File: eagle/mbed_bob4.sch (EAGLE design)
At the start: 15 parts, among them IC1 MBED-SOCKET, K1 651005136521, K2 691210910006, K3 691210910006, T1 2N7002E

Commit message: First working version. To be cleaned up and checked before sending out for production.
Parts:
- added IC2: MAX9934, ic:MAX9934
- added K4: 691210910006, Wuerth_Elektronik_eiCan_14_Terminal_Blocks_WR-TBL_2_0:691210910006
- added R8: R_KELVIN, passives:R_KELVIN
- added X1: SDCARDSHORT, connectors:SDCARDSHORT
- ETH1: value CON-RJ45-F -> CON-RJ45-F_WE100; device dp_devices:CON-RJ45-F -> connectors:CON-RJ45-F_WE100
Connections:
- new net CAN_RX: IC1.30, K4.1
- new net CAN_TX: IC1.29, K4.2
- new net MAX_CS: IC1.22, IC2.CS
- new net N$14: IC1.7, X1.SCK
- new net N$15: IC1.8, X1.CS
- new net N$16: IC1.5, X1.DI
- new net N$17: IC1.6, X1.DO
- new net N$18: IC1.VB
- new net N$19: IC1.NR
- new net N$20: IC1.11
- new net N$21: IC1.12
- new net N$22: IC1.13
- new net N$23: IC1.15
- new net N$24: IC1.16, IC2.OUT
- new net N$25: K3.3, R8.I1
- new net N$26: IC1.23
- new net N$27: IC1.24
- new net N$28: IC1.IF+
- new net N$29: IC1.IF-
- new net N$30: IC1.VU
- new net N$31: IC2.RS-, R8.V2
- new net N$32: IC2.RS+, R8.V1
- new net N$33: K3.4, R8.I2
- new net PWM25: IC1.25, K4.6
- new net PWM26: IC1.26, K4.5
- new net SCL: IC1.27, K4.4
- new net SDA: IC1.28, K4.3
- net +3V3: now also ETH1.CRD, ETH1.CTD, IC2.VCC, X1.VCC; no longer ETH1.4, ETH1.5
- net GND: now also ETH1.GREEN_CATHODE, ETH1.SHIELD, ETH1.YELLOW_CATHODE, IC2.GND, RN2A.1, RN2B.1, RN2C.1, RN2D.1, X1.GND; no longer ETH1.10, ETH1.11
- net LED1: now also IC1.9
- net LED2: now also IC1.10
- net N$1: now also RN2D.2; no longer RN2A.2
- net N$11: now also ETH1.GREEN_ANODE; no longer ETH1.12
- net N$12: now also ETH1.YELLOW_ANODE; no longer ETH1.9
- net N$3: now also IC1.14, X1.CD; no longer RN2A.1, RN2B.1, RN2C.1, RN2D.1
- net N$5: now also RN2A.2; no longer RN2D.2
- net N$6: now also RN2B.2; no longer RN2C.2
- net N$7: now also RN2C.2; no longer RN2B.2
- net RX_N: now also ETH1.RD-; no longer ETH1.6
- net RX_P: now also ETH1.RD+; no longer ETH1.3
- net TX_N: now also ETH1.TD-; no longer ETH1.2
- net TX_P: now also ETH1.TD+; no longer ETH1.1
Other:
- moved on the sheet: ETH1, K1, K2, R1, RN2A, RN2B, RN2C, RN2D, T1

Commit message: Further cleanup
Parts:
- renumbered K1 to USB
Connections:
- removed net N$2: USB.GND
- net +3V3: now also K3.1
- net GND: now also USB.GND
- net N$13: now also K3.4
- net N$25: now also K3.2; no longer K3.3
- net N$33: now also K3.3; no longer K3.4
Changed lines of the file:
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@@
 <parts>
 <part name="FRAME1" library="frames" deviceset="A4L-LOC" device=""/>
-<part name="K1" library="Wuerth_Elektronik_eiCan_11_Communication_Connectors_2_4" deviceset="651005136521" device=""/>
+<part name="USB" library="Wuerth_Elektronik_eiCan_11_Communication_Connectors_2_4" deviceset="651005136521" device=""/>
 <part name="ETH1" library="connectors" deviceset="CON-RJ45-F" device="_WE100"/>
 <part name="GND11" library="mbed-power" deviceset="GND" device=""/>
@@
 <instances>
 <instance part="FRAME1" gate="G$1" x="0" y="0"/>
-<instance part="K1" gate="G$1" x="218.44" y="60.96" rot="MR0"/>
+<instance part="USB" gate="G$1" x="218.44" y="60.96" rot="MR0"/>
 <instance part="ETH1" gate="ETH" x="48.26" y="134.62" rot="MR0"/>
 <instance part="GND11" gate="1" x="228.6" y="48.26" rot="MR0"/>
@@
 <net name="USB_D_N" class="0">
 <segment>
-<pinref part="K1" gate="G$1" pin="D-"/>
+<pinref part="USB" gate="G$1" pin="D-"/>
 <wire x1="226.06" y1="63.5" x2="238.76" y2="63.5" width="0.1524" layer="91"/>
 <label x="231.14" y="63.5" size="1.778" layer="95"/>
@@
 </segment>
 </net>
-<net name="N$2" class="0">
-<segment>
-<pinref part="K1" gate="G$1" pin="GND"/>
-<wire x1="226.06" y1="55.88" x2="228.6" y2="55.88" width="0.1524" layer="91"/>
-</segment>
-</net>
 <net name="USB_D_P" class="0">
 <segment>
-<pinref part="K1" gate="G$1" pin="D+"/>
+<pinref part="USB" gate="G$1" pin="D+"/>
 <wire x1="226.06" y1="60.96" x2="238.76" y2="60.96" width="0.1524" layer="91"/>
 <label x="231.14" y="60.96" size="1.778" layer="95"/>
@@
 <net name="VBUS" class="0">
 <segment>
-<pinref part="K1" gate="G$1" pin="VCC"/>
+<pinref part="USB" gate="G$1" pin="VCC"/>
 <wire x1="226.06" y1="66.04" x2="238.76" y2="66.04" width="0.1524" layer="91"/>
 <label x="231.14" y="66.04" size="1.778" layer="95"/>
@@
 </net>
 <net name="GND" class="0">
-<segment>
-<wire x1="228.6" y1="48.26" x2="228.6" y2="55.88" width="0.1524" layer="91"/>
-<pinref part="GND11" gate="1" pin="GND"/>
-</segment>
 <segment>
 <wire x1="195.58" y1="152.4" x2="190.5" y2="152.4" width="0.1524" layer="91"/>
@@
 <wire x1="114.3" y1="48.26" x2="114.3" y2="50.8" width="0.1524" layer="91"/>
 </segment>
+<segment>
+<pinref part="GND11" gate="1" pin="GND"/>
+<wire x1="228.6" y1="48.26" x2="228.6" y2="55.88" width="0.1524" layer="91"/>
+<pinref part="USB" gate="G$1" pin="GND"/>
+<wire x1="228.6" y1="55.88" x2="226.06" y2="55.88" width="0.1524" layer="91"/>
+</segment>
 </net>
 <net name="+3V3" class="0">
@@
 <wire x1="114.3" y1="73.66" x2="114.3" y2="76.2" width="0.1524" layer="91"/>
 </segment>
+<segment>
+<pinref part="K3" gate="G$1" pin="1"/>
+<pinref part="V3" gate="+3V3" pin="+3V3"/>
+<wire x1="15.24" y1="71.12" x2="17.78" y2="71.12" width="0.1524" layer="91"/>
+<wire x1="17.78" y1="71.12" x2="17.78" y2="76.2" width="0.1524" layer="91"/>
+</segment>
 </net>
 <net name="LGC_IN_LV" class="0">
@@
 <pinref part="T1" gate="A" pin="G"/>
 <pinref part="K3" gate="G$1" pin="5"/>
-<wire x1="15.24" y1="60.96" x2="22.86" y2="60.96" width="0.1524" layer="91"/>
+<wire x1="15.24" y1="60.96" x2="17.78" y2="60.96" width="0.1524" layer="91"/>
+<wire x1="17.78" y1="60.96" x2="22.86" y2="60.96" width="0.1524" layer="91"/>
 <wire x1="22.86" y1="60.96" x2="22.86" y2="22.86" width="0.1524" layer="91"/>
 <wire x1="22.86" y1="22.86" x2="25.4" y2="22.86" width="0.1524" layer="91"/>
+<pinref part="K3" gate="G$1" pin="4"/>
+<wire x1="15.24" y1="63.5" x2="17.78" y2="63.5" width="0.1524" layer="91"/>
+<wire x1="17.78" y1="63.5" x2="17.78" y2="60.96" width="0.1524" layer="91"/>
+<junction x="17.78" y="60.96"/>
 </segment>
 </net>
@@
 <net name="N$25" class="0">
 <segment>
-<pinref part="K3" gate="G$1" pin="3"/>
-<wire x1="15.24" y1="66.04" x2="40.64" y2="66.04" width="0.1524" layer="91"/>
-<wire x1="40.64" y1="66.04" x2="40.64" y2="73.66" width="0.1524" layer="91"/>
 <pinref part="R8" gate="G$1" pin="I1"/>
+<wire x1="40.64" y1="68.58" x2="40.64" y2="73.66" width="0.1524" layer="91"/>
 <wire x1="40.64" y1="73.66" x2="48.26" y2="73.66" width="0.1524" layer="91"/>
+<pinref part="K3" gate="G$1" pin="2"/>
+<wire x1="15.24" y1="68.58" x2="40.64" y2="68.58" width="0.1524" layer="91"/>
 </segment>
 </net>
@@
 <wire x1="73.66" y1="73.66" x2="73.66" y2="60.96" width="0.1524" layer="91"/>
 <wire x1="73.66" y1="60.96" x2="27.94" y2="60.96" width="0.1524" layer="91"/>
-<wire x1="27.94" y1="60.96" x2="27.94" y2="63.5" width="0.1524" layer="91"/>
-<pinref part="K3" gate="G$1" pin="4"/>
-<wire x1="27.94" y1="63.5" x2="15.24" y2="63.5" width="0.1524" layer="91"/>
+<wire x1="27.94" y1="60.96" x2="27.94" y2="66.04" width="0.1524" layer="91"/>
+<pinref part="K3" gate="G$1" pin="3"/>
+<wire x1="27.94" y1="66.04" x2="15.24" y2="66.04" width="0.1524" layer="91"/>
 </segment>
 </net>
@@
 </sheet>
 </sheets>
+<errors>
+</errors>
 </schematic>
 </drawing>

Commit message: Final version before boardout.
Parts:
- added C2: (no value), passives:C0805_RFLW
- added R10, R9: (no value), passives:R0805_RFLW
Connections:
- net GND: now also C2.1, R10.1, R9.1
- net N$13: now also R10.2
- net N$24: now also C2.2, R9.2
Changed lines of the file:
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@@
 <part name="GND10" library="mbed-power" deviceset="GND" device=""/>
 <part name="V7" library="netnode" deviceset="+3V3" device=""/>
+<part name="R9" library="passives" deviceset="R" device="" technology="0805_RFLW"/>
+<part name="C2" library="passives" deviceset="C" device="0805_RFLW"/>
+<part name="GND12" library="mbed-power" deviceset="GND" device=""/>
+<part name="R10" library="passives" deviceset="R" device="" technology="0805_RFLW"/>
 </parts>
 <sheets>
@@
 <instance part="GND10" gate="1" x="114.3" y="48.26" rot="MR0"/>
 <instance part="V7" gate="+3V3" x="114.3" y="78.74"/>
+<instance part="R9" gate="G$1" x="121.92" y="101.6" rot="R90"/>
+<instance part="C2" gate="G$1" x="114.3" y="99.06" rot="R180"/>
+<instance part="GND12" gate="1" x="119.38" y="93.98" rot="MR0"/>
+<instance part="R10" gate="G$1" x="22.86" y="17.78" rot="R90"/>
 </instances>
 <busses>
@@
 <pinref part="GND2" gate="1" pin="GND"/>
 <wire x1="38.1" y1="12.7" x2="38.1" y2="15.24" width="0.1524" layer="91"/>
+<pinref part="R10" gate="G$1" pin="1"/>
+<wire x1="38.1" y1="12.7" x2="22.86" y2="12.7" width="0.1524" layer="91"/>
+<junction x="38.1" y="12.7"/>
 </segment>
 <segment>
@@
 <wire x1="228.6" y1="55.88" x2="226.06" y2="55.88" width="0.1524" layer="91"/>
 </segment>
+<segment>
+<pinref part="C2" gate="G$1" pin="1"/>
+<wire x1="114.3" y1="96.52" x2="114.3" y2="93.98" width="0.1524" layer="91"/>
+<wire x1="114.3" y1="93.98" x2="119.38" y2="93.98" width="0.1524" layer="91"/>
+<pinref part="R9" gate="G$1" pin="1"/>
+<wire x1="119.38" y1="93.98" x2="121.92" y2="93.98" width="0.1524" layer="91"/>
+<wire x1="121.92" y1="93.98" x2="121.92" y2="96.52" width="0.1524" layer="91"/>
+<pinref part="GND12" gate="1" pin="GND"/>
+<junction x="119.38" y="93.98"/>
+</segment>
 </net>
 <net name="+3V3" class="0">
@@
 <wire x1="17.78" y1="63.5" x2="17.78" y2="60.96" width="0.1524" layer="91"/>
 <junction x="17.78" y="60.96"/>
+<pinref part="R10" gate="G$1" pin="2"/>
+<junction x="22.86" y="22.86"/>
 </segment>
 </net>
@@
 <pinref part="IC2" gate="G$1" pin="OUT"/>
 <wire x1="129.54" y1="60.96" x2="137.16" y2="60.96" width="0.1524" layer="91"/>
-<wire x1="137.16" y1="60.96" x2="137.16" y2="114.3" width="0.1524" layer="91"/>
+<wire x1="137.16" y1="60.96" x2="137.16" y2="109.22" width="0.1524" layer="91"/>
+<wire x1="137.16" y1="109.22" x2="137.16" y2="114.3" width="0.1524" layer="91"/>
 <wire x1="137.16" y1="114.3" x2="195.58" y2="114.3" width="0.1524" layer="91"/>
-</segment>
-</net>
+<pinref part="C2" gate="G$1" pin="2"/>
+<wire x1="137.16" y1="109.22" x2="121.92" y2="109.22" width="0.1524" layer="91"/>
+<wire x1="121.92" y1="109.22" x2="114.3" y2="109.22" width="0.1524" layer="91"/>
+<wire x1="114.3" y1="109.22" x2="114.3" y2="104.14" width="0.1524" layer="91"/>
+<junction x="137.16" y="109.22"/>
+<pinref part="R9" gate="G$1" pin="2"/>
+<wire x1="121.92" y1="106.68" x2="121.92" y2="109.22" width="0.1524" layer="91"/>
+<junction x="121.92" y="109.22"/>
+</segment>
+</net>

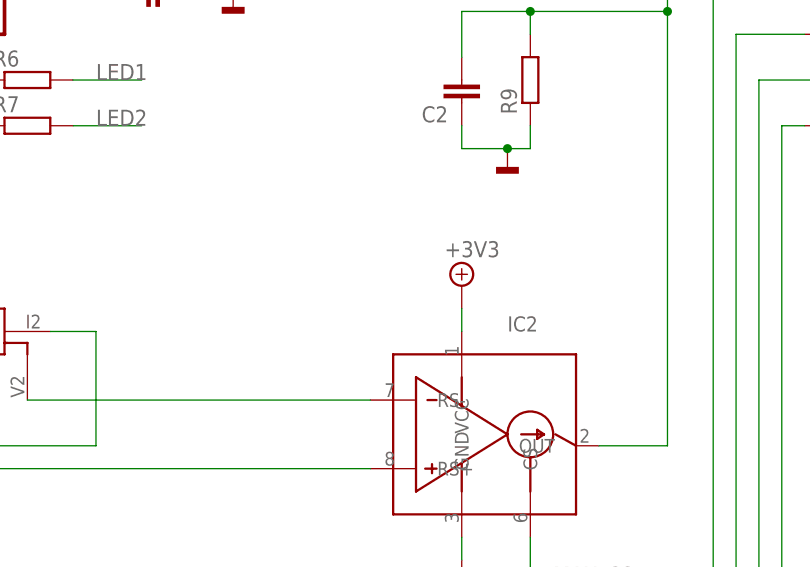
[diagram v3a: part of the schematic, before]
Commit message: Added decoupling resistor.
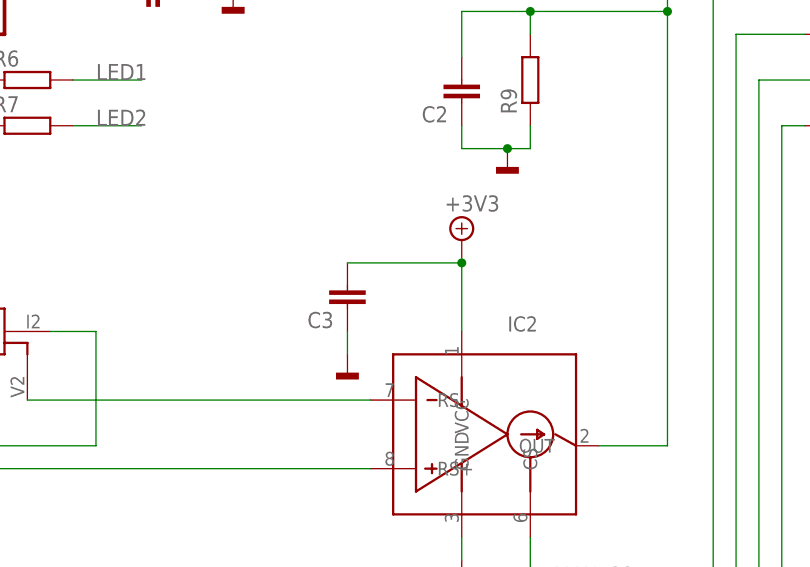
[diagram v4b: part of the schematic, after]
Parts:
- added C3: (no value), passives:C0805_RFLW
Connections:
- net +3V3: now also C3.2
- net GND: now also C3.1
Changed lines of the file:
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@@
 <part name="GND12" library="mbed-power" deviceset="GND" device=""/>
 <part name="R10" library="passives" deviceset="R" device="" technology="0805_RFLW"/>
+<part name="C3" library="passives" deviceset="C" device="0805_RFLW"/>
+<part name="GND13" library="mbed-power" deviceset="GND" device=""/>
 </parts>
 <sheets>
@@
 <instance part="IC2" gate="G$1" x="114.3" y="60.96"/>
 <instance part="GND10" gate="1" x="114.3" y="48.26" rot="MR0"/>
-<instance part="V7" gate="+3V3" x="114.3" y="78.74"/>
+<instance part="V7" gate="+3V3" x="114.3" y="83.82"/>
 <instance part="R9" gate="G$1" x="121.92" y="101.6" rot="R90"/>
 <instance part="C2" gate="G$1" x="114.3" y="99.06" rot="R180"/>
 <instance part="GND12" gate="1" x="119.38" y="93.98" rot="MR0"/>
 <instance part="R10" gate="G$1" x="22.86" y="17.78" rot="R90"/>
+<instance part="C3" gate="G$1" x="101.6" y="76.2" rot="R180"/>
+<instance part="GND13" gate="1" x="101.6" y="71.12" rot="MR0"/>
 </instances>
 <busses>
@@
 <junction x="119.38" y="93.98"/>
 </segment>
+<segment>
+<pinref part="C3" gate="G$1" pin="1"/>
+<pinref part="GND13" gate="1" pin="GND"/>
+<wire x1="101.6" y1="71.12" x2="101.6" y2="73.66" width="0.1524" layer="91"/>
+</segment>
 </net>
 <net name="+3V3" class="0">
@@
 <pinref part="IC2" gate="G$1" pin="VCC"/>
 <pinref part="V7" gate="+3V3" pin="+3V3"/>
-<wire x1="114.3" y1="73.66" x2="114.3" y2="76.2" width="0.1524" layer="91"/>
-</segment>
-<segment>
+<wire x1="114.3" y1="73.66" x2="114.3" y2="81.28" width="0.1524" layer="91"/>
+<pinref part="C3" gate="G$1" pin="2"/>
+<wire x1="101.6" y1="81.28" x2="114.3" y2="81.28" width="0.1524" layer="91"/>
+<junction x="114.3" y="81.28"/>
+</segment>
+<segment>
